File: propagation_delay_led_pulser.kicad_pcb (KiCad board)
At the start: 2 copper layers, 19 parts, among them J1 Conn_01x03, J2 Conn_01x02, J3 Conn_Coaxial, J4 Conn_Coaxial, J5 Conn_Coaxial, J6 Conn_01x02, U1 LTC1799, U2 74AC14, U3 74AHC1G00

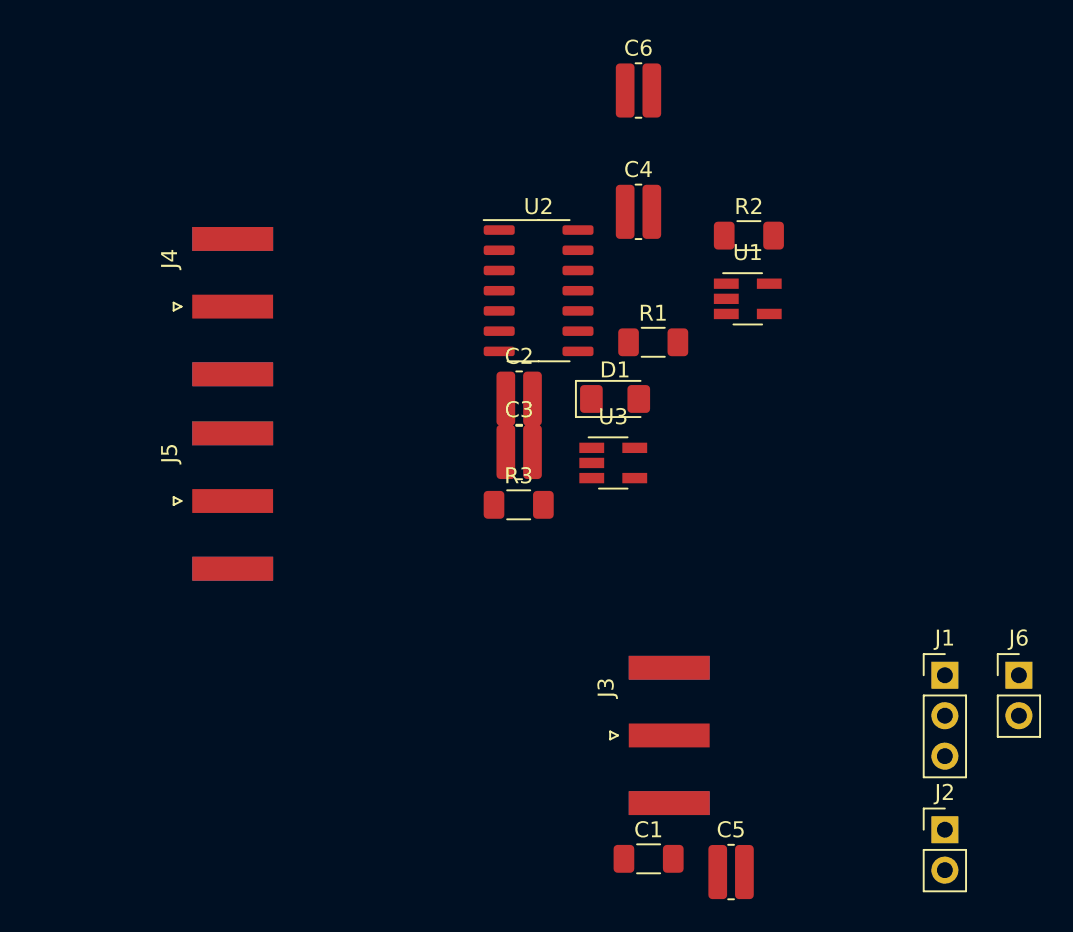
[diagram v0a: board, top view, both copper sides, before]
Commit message: Changed headers to one nano-fit
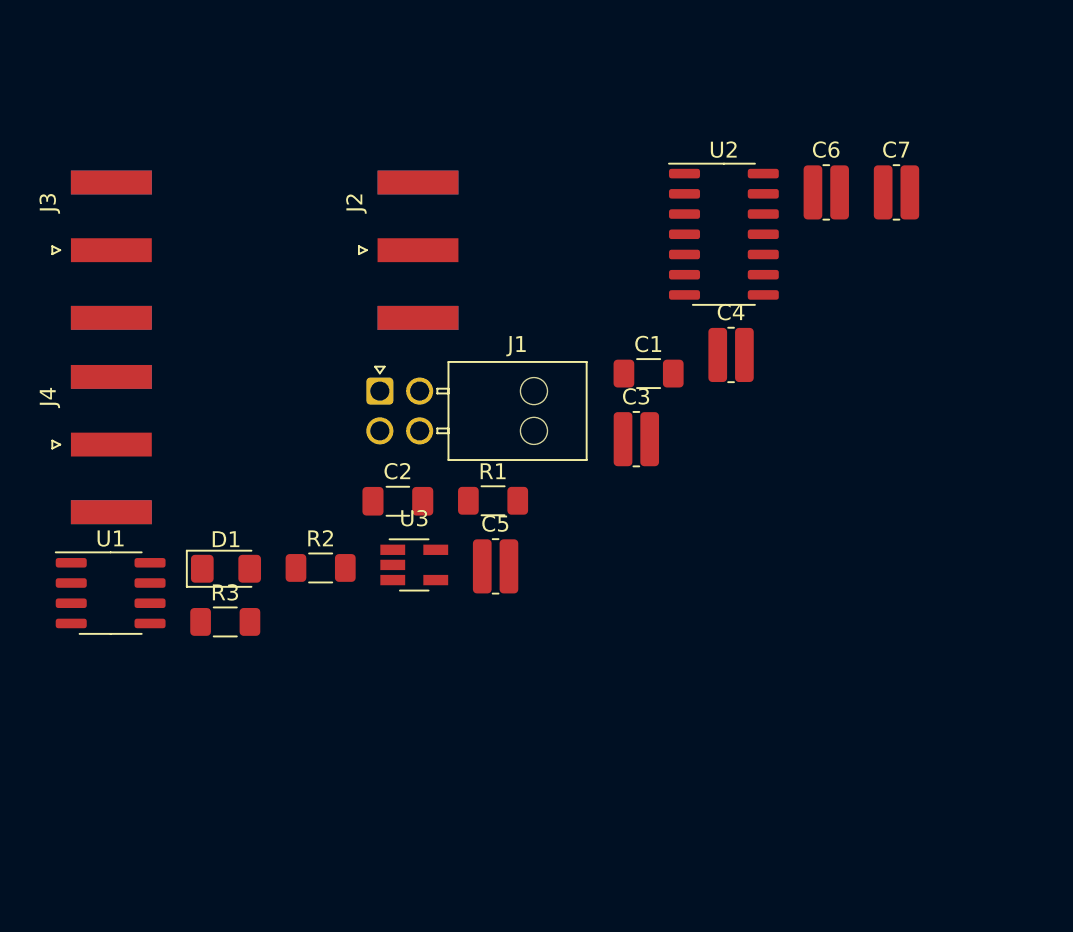
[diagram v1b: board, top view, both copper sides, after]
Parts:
- removed J5: Conn_Coaxial, Connector_Coaxial:SMA_Amphenol_132289_EdgeMount
- removed J6: Conn_01x02, Connector_PinHeader_2.54mm:PinHeader_1x02_P2.54mm_Vertical
- added C7: 1u, Resistor_SMD:R_0612_1632Metric_Pad1.18x3.40mm_HandSolder, F.Cu at (166.7, 87.0)
- C2: value 0.1u -> 1n; footprint Resistor_SMD:R_0612_1632Metric_Pad1.18x3.40mm_HandSolder -> Capacitor_SMD:C_1206_3216Metric_Pad1.33x1.80mm_HandSolder
- C6: value 1u -> 0.1u
- J1: value Conn_01x03 -> Power/Bias In; footprint Connector_PinHeader_2.54mm:PinHeader_1x03_P2.54mm_Vertical -> Connector_Molex:Molex_Nano-Fit_105314-xx04_2x02_P2.50mm_Horizontal
- J2: value Conn_01x02 -> Anode Bias In; footprint Connector_PinHeader_2.54mm:PinHeader_1x02_P2.54mm_Vertical -> Connector_Coaxial:SMA_Amphenol_132289_EdgeMount
- J3: value Conn_Coaxial -> Power In
- J4: value Conn_Coaxial -> Pulse Out
- R1: value 1M -> 72K
- U1: value LTC1799 -> ICM7555xB; footprint Package_TO_SOT_SMD:SOT-23-5_HandSoldering -> Package_SO:SOIC-8_3.9x4.9mm_P1.27mm
- moved J2 49.2 mm to (136.6, 90.7)
- moved J3 46.4 mm to (117.4, 90.7)
- moved U1 44.1 mm to (117.3, 112.2)
- moved J1 39.7 mm to (134.2, 99.5)
- moved R2 34.0 mm to (130.5, 110.6)
- moved C1 30.5 mm to (151.1, 98.4)
- moved D1 26.7 mm to (124.6, 110.7)
- moved C5 24.2 mm to (141.5, 110.5)
- moved R3 19.8 mm to (124.5, 114.0)
- moved R1 14.2 mm to (141.4, 106.4)
- moved U3 14.0 mm to (136.4, 110.4)
- moved C6 13.4 mm to (162.3, 87.0)
- moved U2 12.2 mm to (155.9, 89.7)
- moved J4 11.5 mm to (117.4, 102.9)
- moved C4 10.7 mm to (156.3, 97.3)
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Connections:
- net Net-(U2-Pad11) renamed /Pulser_out
- C2 pad 1: VCC -> /Timer_THR
- C6 pad 1: Net-(C6-Pad1) -> VCC
- D1 pad 1: Net-(C6-Pad1) -> /LED_Anode
- J1 pad 1: VDC -> VCC
- J1 pad 2: Net-(J1-Pad2) -> /LED_Anode
- J2 pad 1: VCC -> /LED_Anode
- R1 pad 1: VCC -> /Timer_out
- R1 pad 2: Net-(R1-Pad2) -> /Timer_THR
- U1 pad 1: VCC -> GND
- U1 pad 2: GND -> /Timer_THR
- U1 pad 3: Net-(R1-Pad2) -> /Timer_out
- U1 pad 4: Net-(J1-Pad2) -> VCC
- U1 pad 5: Net-(U1-Pad5) -> unconnected-(U1-Pad5)
- U2 pad 1: Net-(U1-Pad5) -> /Timer_out
- U3 pad 1: Net-(U1-Pad5) -> /Timer_out

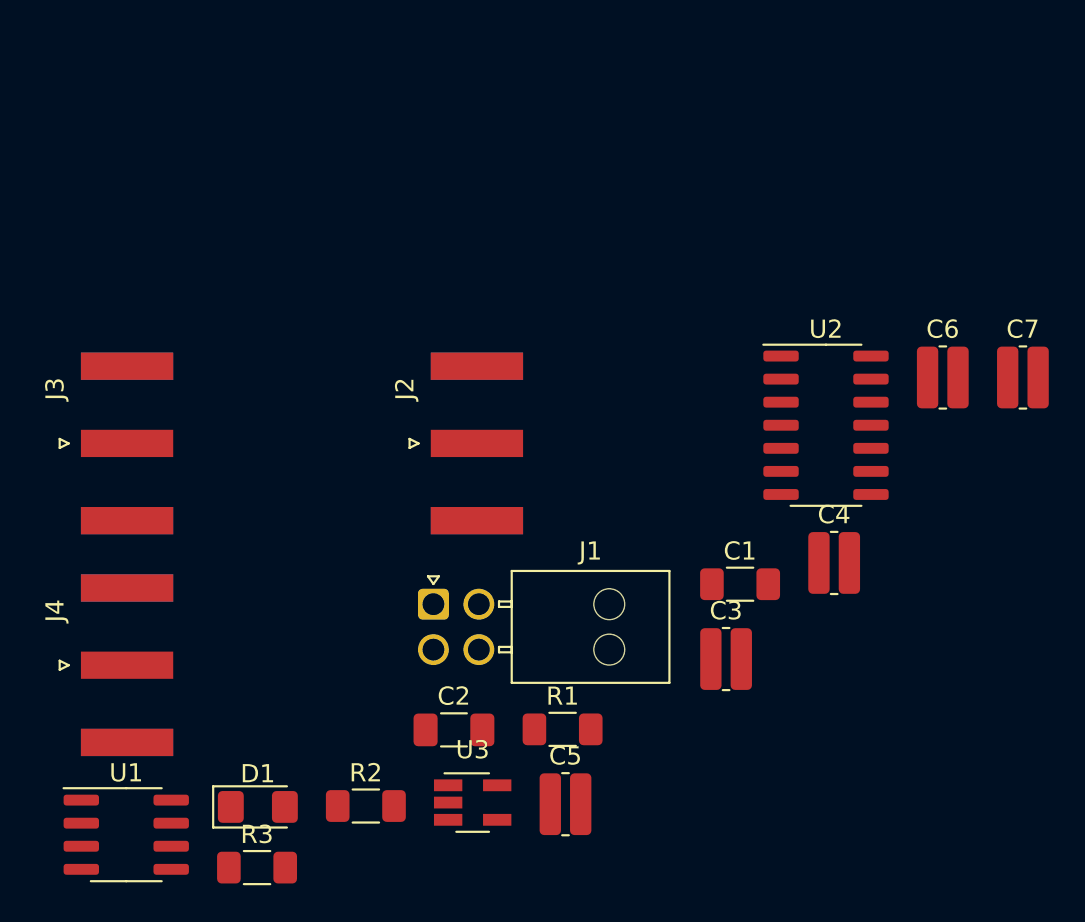
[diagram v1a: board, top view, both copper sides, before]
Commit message: removed pwr/bias SMAs and initial PCB placement
  also added mfr/part for timer capacitor
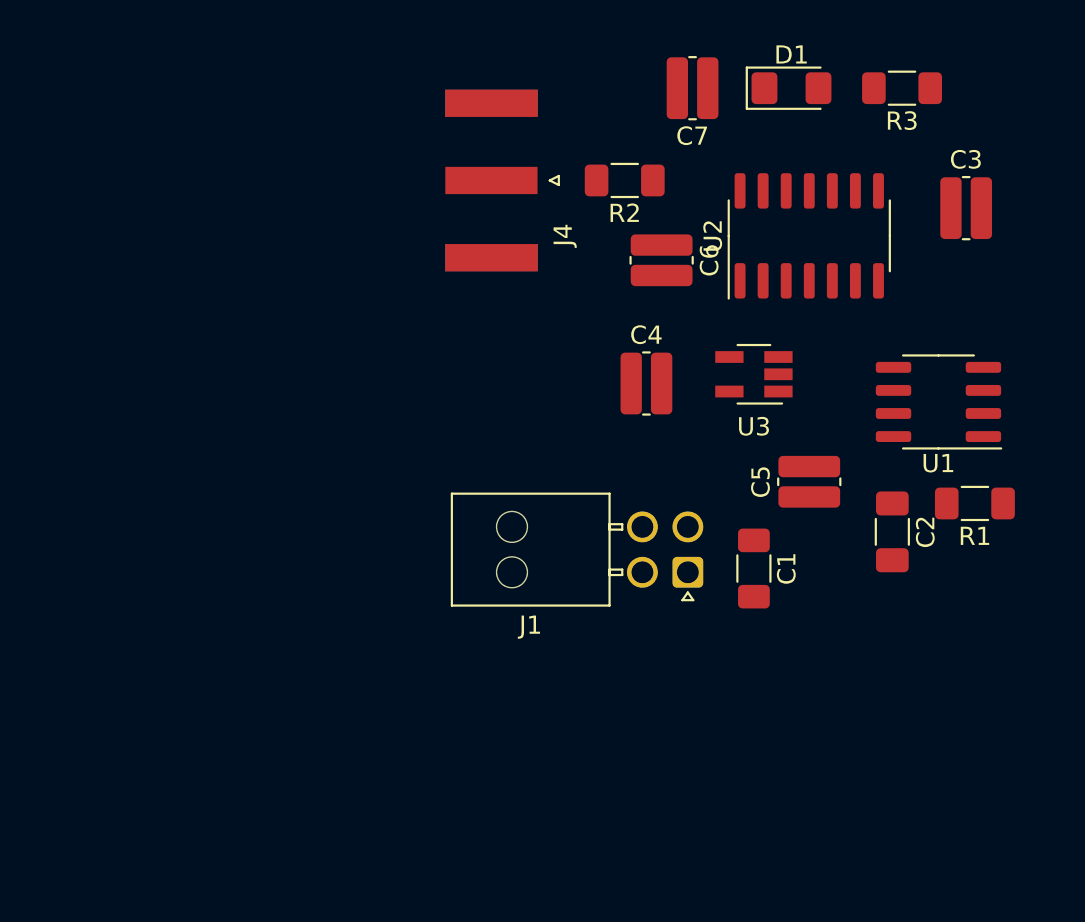
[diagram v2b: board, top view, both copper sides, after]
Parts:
- removed J2: Anode Bias In, Connector_Coaxial:SMA_Amphenol_132289_EdgeMount
- removed J3: Power In, Connector_Coaxial:SMA_Amphenol_132289_EdgeMount
- moved R3 55.7 mm to (160.0, 71.1), turned to 180 degrees
- moved U1 50.7 mm to (162.1, 88.4), turned to 180 degrees
- moved D1 49.3 mm to (154.0, 71.1)
- moved R2 37.3 mm to (144.8, 76.2), turned to 180 degrees
- moved J4 33.4 mm to (137.4, 76.2), turned to 180 degrees
- moved U3 28.2 mm to (151.9, 86.9), turned to 180 degrees
- moved C3 28.1 mm to (163.6, 77.7)
- moved C2 26.5 mm to (159.5, 95.5), turned to -90 degrees
- moved R1 25.9 mm to (164.1, 94.0), turned to 180 degrees
- moved C7 24.2 mm to (148.5, 71.1), turned to 180 degrees
- moved C5 22.3 mm to (154.9, 92.8), turned to 90 degrees
- moved C6 16.8 mm to (146.8, 80.6), turned to -90 degrees
- moved C4 14.3 mm to (146.0, 87.4)
- moved J1 14.1 mm to (148.3, 97.8), turned to 180 degrees
- moved U2 10.5 mm to (154.9, 79.2), turned to 90 degrees
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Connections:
- net Net-(U2-Pad2) renamed /Inv1to2
- net Net-(U2-Pad4) renamed /Inv2to3
- net Net-(U2-Pad6) renamed /Inv3toNand
- R2 pad 1: Net-(R2-Pad1) -> /drive_pulse_out_r
- R3 pad 1: Net-(R3-Pad1) -> /drive_led_r
- U2 pad 10: Net-(R2-Pad1) -> /drive_pulse_out_r
- U2 pad 12: Net-(R3-Pad1) -> /drive_pulse_out_r
- U2 pad 14: (no net) -> VCC
- U2 pad 7: (no net) -> GND
- U2 pad 8: Net-(R2-Pad1) -> /drive_led_r

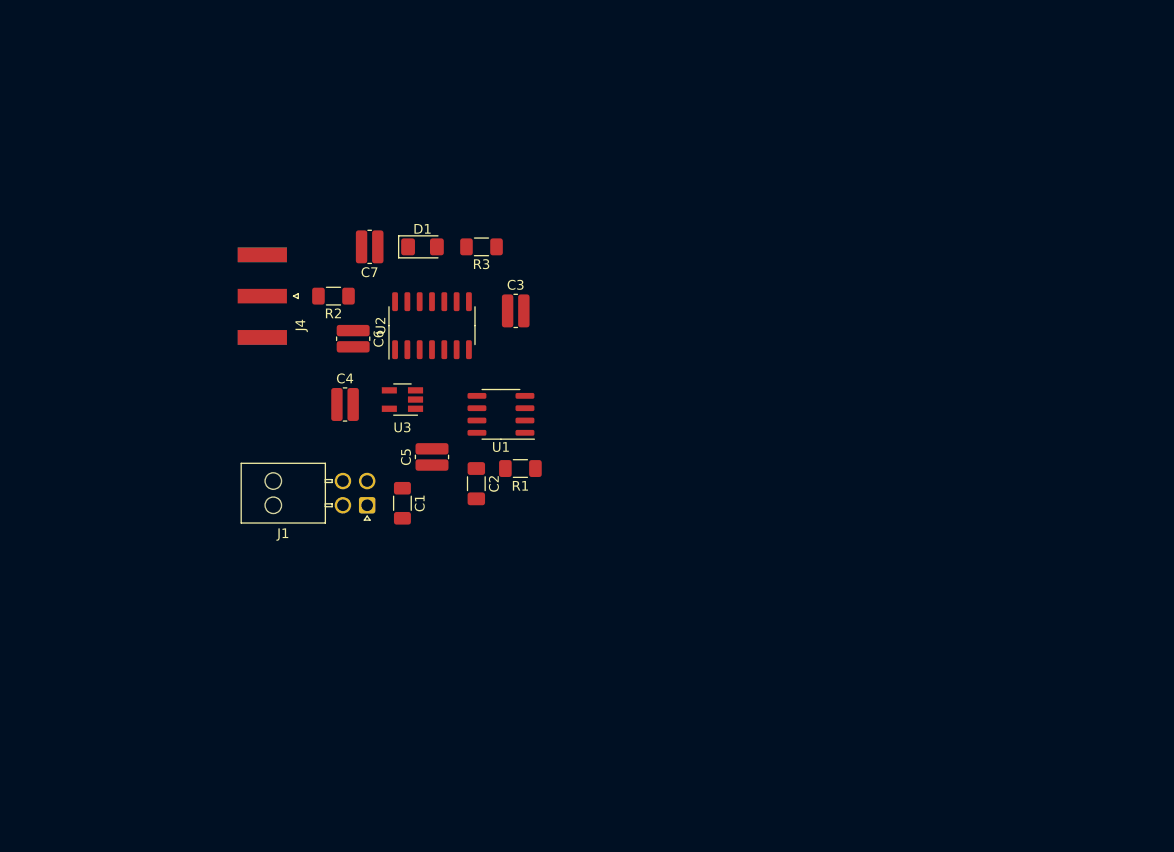
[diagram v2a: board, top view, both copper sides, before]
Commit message: Added board outline
  aligned connectors with outline
  added power for inverter to schematic
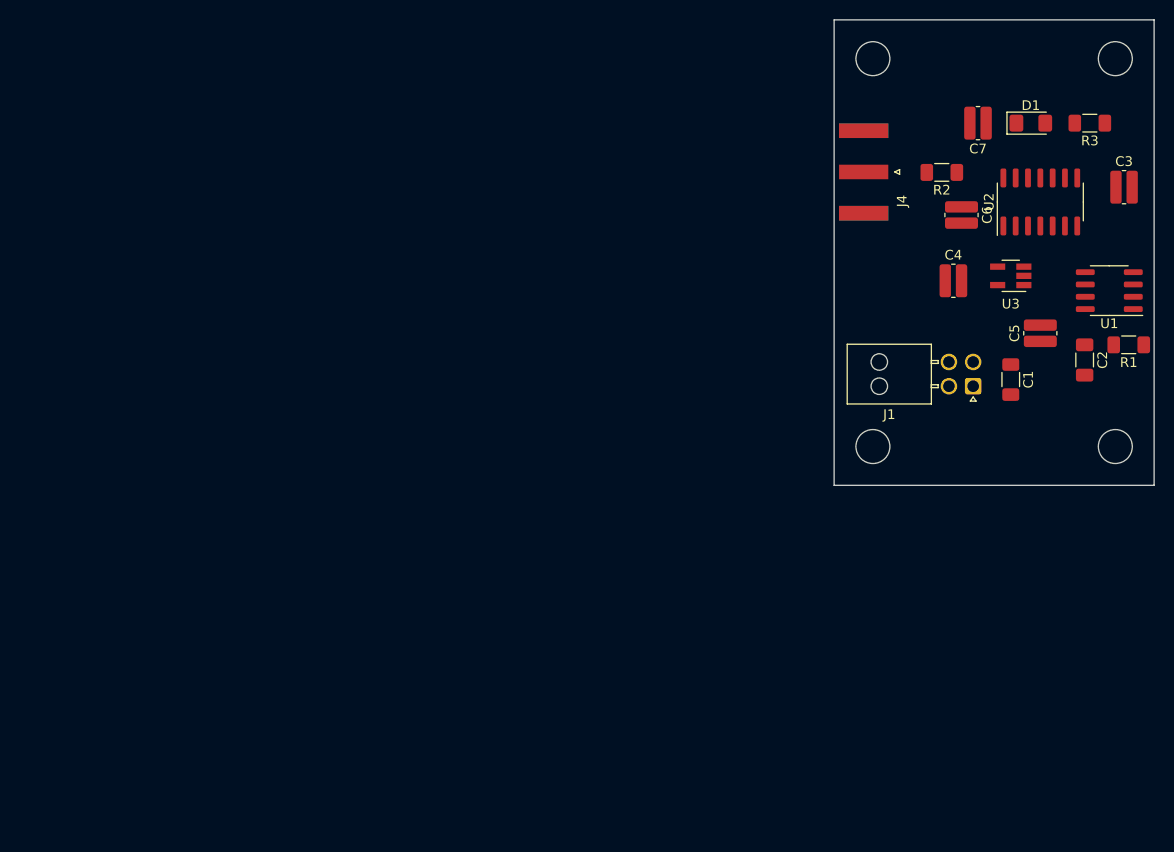
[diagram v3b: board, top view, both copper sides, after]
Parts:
- moved C1 64.0 mm to (214.6, 84.8)
- moved C2 64.0 mm to (222.2, 82.8)
- moved C3 64.0 mm to (226.3, 65.0)
- moved C5 64.0 mm to (217.7, 80.0)
- moved C7 64.0 mm to (211.2, 58.4)
- moved D1 64.0 mm to (216.7, 58.4)
- moved R1 64.0 mm to (226.8, 81.2)
- moved R3 64.0 mm to (222.8, 58.4)
- moved U1 64.0 mm to (224.8, 75.6)
- moved U2 64.0 mm to (217.7, 66.5)
- moved U3 64.0 mm to (214.6, 74.1)
- moved C4 64.0 mm to (208.7, 74.6)
- moved C6 64.0 mm to (209.5, 67.8)
- moved R2 64.0 mm to (207.5, 63.4)
- moved J1 63.7 mm to (210.8, 85.5)
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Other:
- board outline added: 33 x 48 mm
- board text added: "0"
- board text added: "0 mm"
- board text added: "0.0000 mm x 0.0000 mm"
- board text added: "0.01 mm"
- board text added: "0.02"
- board text added: "0.035 mm"
- board text added: "0.2000 mm / 0.0000 mm"
- board text added: "0.3000 mm"
- board text added: "1"
- board text added: "1.51 mm"
- board text added: "1.6000 mm"
- board text added: "2"
- board text added: "3.3"
- board text added: "4.5"
- board text added: "B.Cu"
- board text added: "B.Mask"
- board text added: "B.Paste"
- board text added: "B.Silkscreen"
- board text added: "BOARD CHARACTERISTICS"
- board text added: "Board Thickness:"
- board text added: "Board overall dimensions:"
- board text added: "Bottom Silk Screen"
- board text added: "Bottom Solder Mask"
- board text added: "Bottom Solder Paste"
- board text added: "Castellated pads:"
- board text added: "Color"
- board text added: "Copper Finish:"
- board text added: "Copper Layer Count:"
- board text added: "Dielectric"
- board text added: "Edge card connectors:"
- board text added: "Epsilon R"
- board text added: "F.Cu"
- board text added: "F.Mask"
- board text added: "F.Paste"
- board text added: "F.Silkscreen"
- board text added: "FR4"
- board text added: "Impedance Control:"
- board text added: "Layer Name"
- board text added: "Loss Tangent"
- board text added: "Material"
- board text added: "Min hole diameter:"
- board text added: "Min track/spacing:"
- board text added: "No"
- board text added: "None"
- board text added: "Not specified"
- board text added: "Plated Board Edge:"
- board text added: "Thickness (mm)"
- board text added: "Top Silk Screen"
- board text added: "Top Solder Mask"
- board text added: "Top Solder Paste"
- board text added: "Type"
- board text added: "copper"
- board text added: "core"
